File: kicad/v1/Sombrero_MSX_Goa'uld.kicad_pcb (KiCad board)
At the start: 2 copper layers, 53.3 x 81.3 mm, 16 parts, among them J1 Z80CPU, U1 74HCT373, U2 74HCT373, U3 SN74LVC245AN, U4 SN74LVC245AN, U5 SN74LVC245AN, U6 Tang_Nano_20k

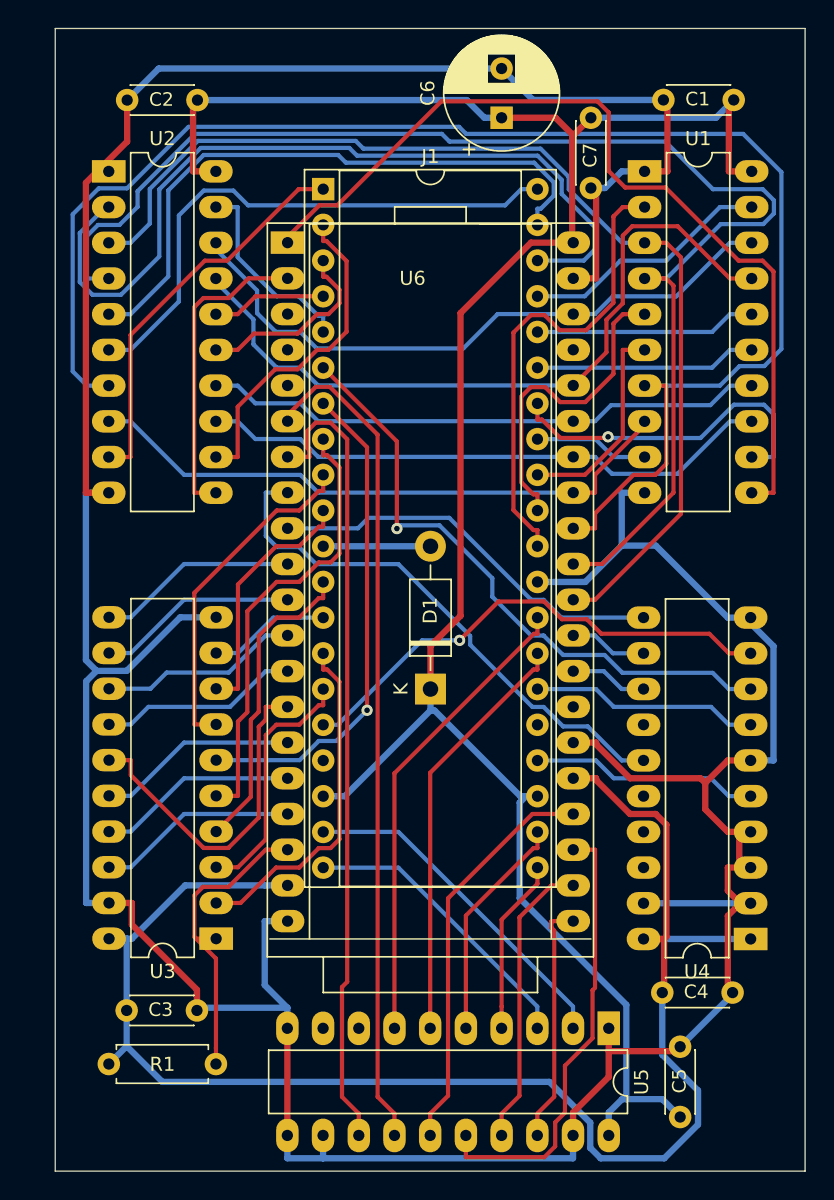
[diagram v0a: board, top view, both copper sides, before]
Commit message: HW Version 1.4 -Included resistor array -Replaced U1, U2 -> 74HC373, U5 -> 74HC245 -Removed capacitor, resistor -Reduced size
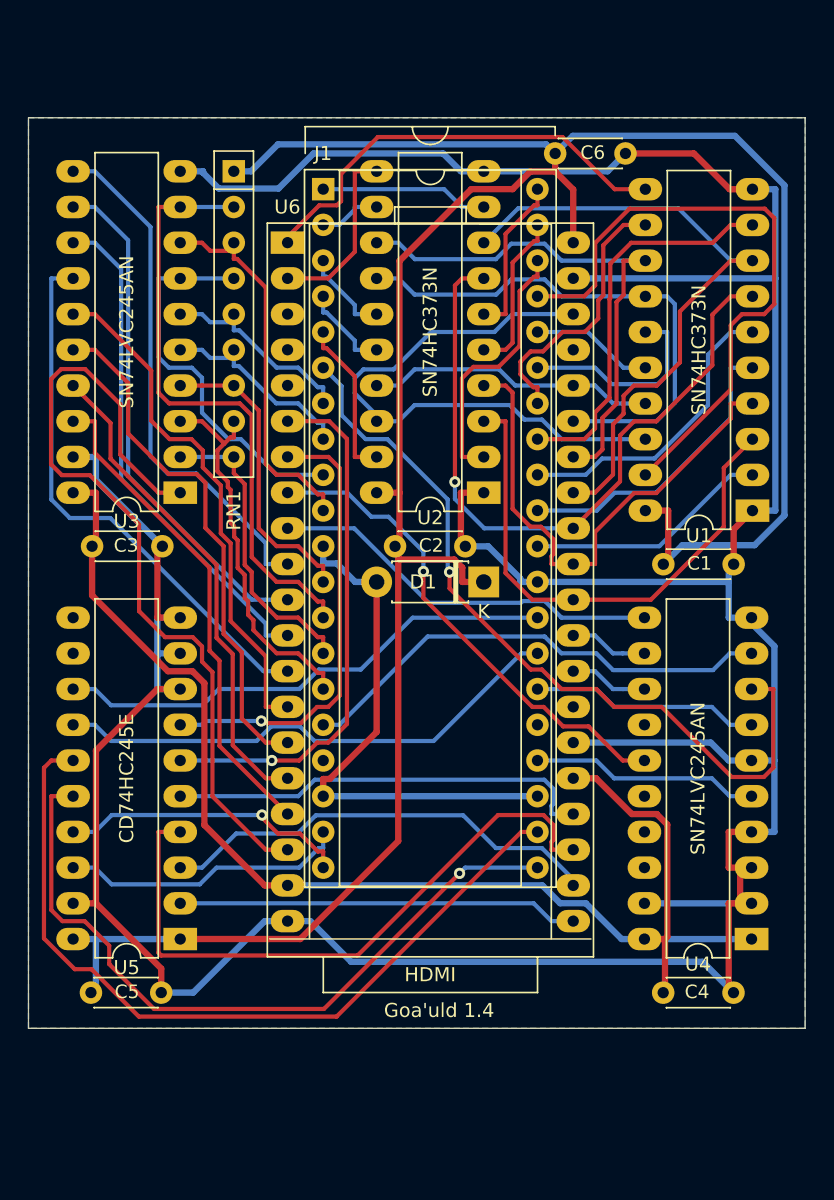
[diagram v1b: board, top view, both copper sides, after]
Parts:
- removed the C6 at (152.4, 71.1)
- removed R1: 10k, Resistor_THT:R_Axial_DIN0207_L6.3mm_D2.5mm_P7.62mm_Horizontal
- added RN1: R_Network08, Resistor_THT:R_Array_SIP9, F.Cu at (133.3, 74.9)
- D1: footprint Diode_THT:D_DO-41_SOD81_P10.16mm_Horizontal -> Diode_THT:D_DO-41_SOD81_P7.62mm_Horizontal
- U1, U2: value 74HCT373 -> SN74HC373N
- U5: value SN74LVC245AN -> CD74HC245E
- moved C5 42.8 mm to (123.2, 133.3), turned to 0 degrees
- moved U2 35.1 mm to (151.1, 97.8), turned to 180 degrees
- moved C2 34.7 mm to (144.8, 101.6), turned to 0 degrees
- moved C1 33.4 mm to (163.9, 102.9), turned to 0 degrees
- moved C3 33.1 mm to (123.3, 101.6)
- moved U3 31.8 mm to (129.5, 97.8)
- moved U5 31.1 mm to (129.5, 129.5), turned to 180 degrees
- moved U1 25.3 mm to (170.2, 99.1), turned to 180 degrees
- moved D1 8.51 mm to (151.1, 104.1), turned to 180 degrees
- moved C6 3.59 mm to (156.2, 73.7), turned to 0 degrees
- moved C4 0.07 mm to (163.9, 133.4)
- moved U4 0.07 mm to (170.2, 129.5)
- renumbered C7 to C6
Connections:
- D1 pad 2: VCC -> VCC_5V
- J1 pad 11: VCC -> VCC_5V
- J1 pad 17: NMI -> unconnected-(J1-Pad17)
- J1 pad 18: VCC_4V7 -> VCC_5V
- J1 pad 23: VCC_4V7 -> VCC_5V
- J1 pad 25: BUSRQ -> unconnected-(J1-Pad25)
- U5 pad 1: GND -> VCC_4V7
- U5 pad 11: GND -> unconnected-(U5-Pad11)
- U5 pad 12: GND -> unconnected-(U5-Pad12)
- U5 pad 13: RFSH_33 -> RFSH
- U5 pad 14: M1_33 -> M1
- U5 pad 15: WR_33 -> WR
- U5 pad 16: RD_33 -> RD
- U5 pad 17: IORQ_33 -> IORQ
- U5 pad 18: MERQ_33 -> MERQ
- U5 pad 2: MERQ -> MERQ_33
- U5 pad 3: IORQ -> IORQ_33
- U5 pad 4: RD -> RD_33
- U5 pad 5: WR -> WR_33
- U5 pad 6: M1 -> M1_33
- U5 pad 7: RFSH -> RFSH_33
- U5 pad 8: unconnected-(U5-Pad8) -> GND
- U5 pad 9: unconnected-(U5-Pad9) -> GND
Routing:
- net MP1_33: track 97.3 -> 37.2 mm
- net MP2_33: track 108.1 -> 50.3 mm, vias 0 -> 1
- net WR: track 16.2 -> 57.3 mm
- net A8: track 59.4 -> 18.9 mm
- net MP0_33: track 77.5 -> 37.9 mm
- net RD: track 12.5 -> 52.1 mm, vias 0 -> 1
- net VCC_5V: track 0.00 -> 37.9 mm
- net DATADIR_33: track 22.0 -> 58.9 mm
- net D7: track 8.66 -> 43.5 mm
- net A9: track 44.4 -> 11.5 mm
- net MP6_33: track 52.9 -> 20.6 mm
- net MSEL0_33: track 63.7 -> 31.5 mm
- net VCC_4V7: track 153.6 -> 182.3 mm
- net A10: track 39.7 -> 11.5 mm
- net A7: track 17.9 -> 44.5 mm
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- added copper zone on B.Cu, net GND
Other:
- board size 53.3 x 81.3 mm -> 55.2 x 64.8 mm
- board text added: "Goa'uld 1.4"
- board text added: "HDMI"
